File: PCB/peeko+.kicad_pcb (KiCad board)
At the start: 2 copper layers, 52.1 x 43.2 mm, 31 parts, among them J1 Rasberry PI Pico, J2 Conn_02x15_Odd_Even, J3 Conn_01x02_Pin, J4 Conn_01x02_Pin, U1 TXU0104, U2 TXU0104, U3 TXU0104, U4 TXU0104, U5 TXU0104, U6 TXU0104

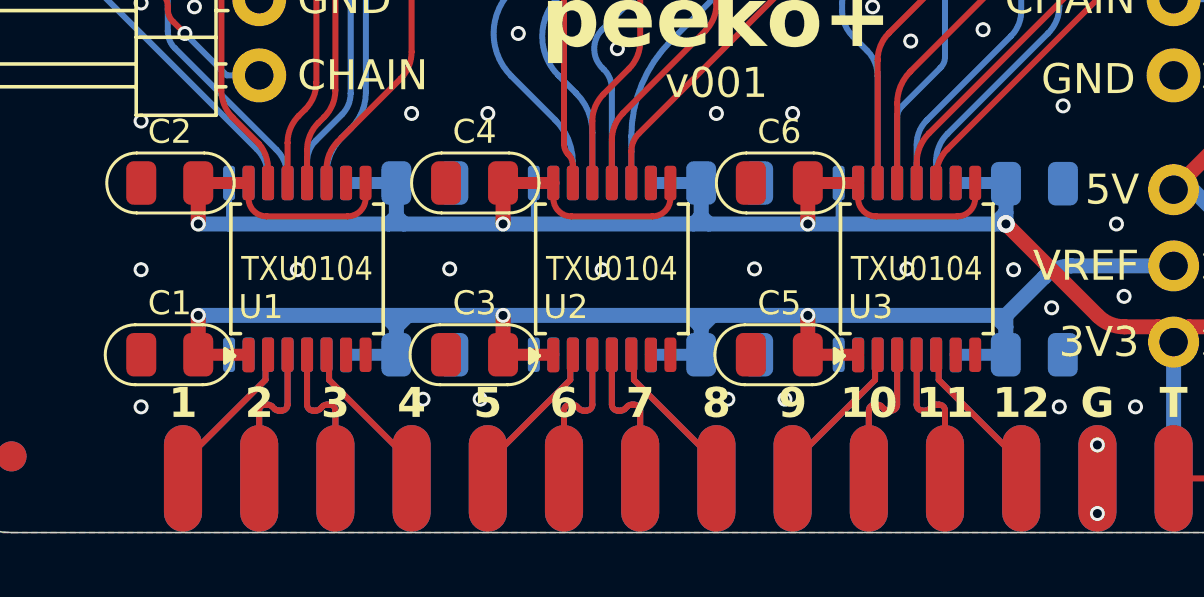
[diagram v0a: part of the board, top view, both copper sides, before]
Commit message: local tssop14 footprint, redo short side traces on peeko+ & level shifter
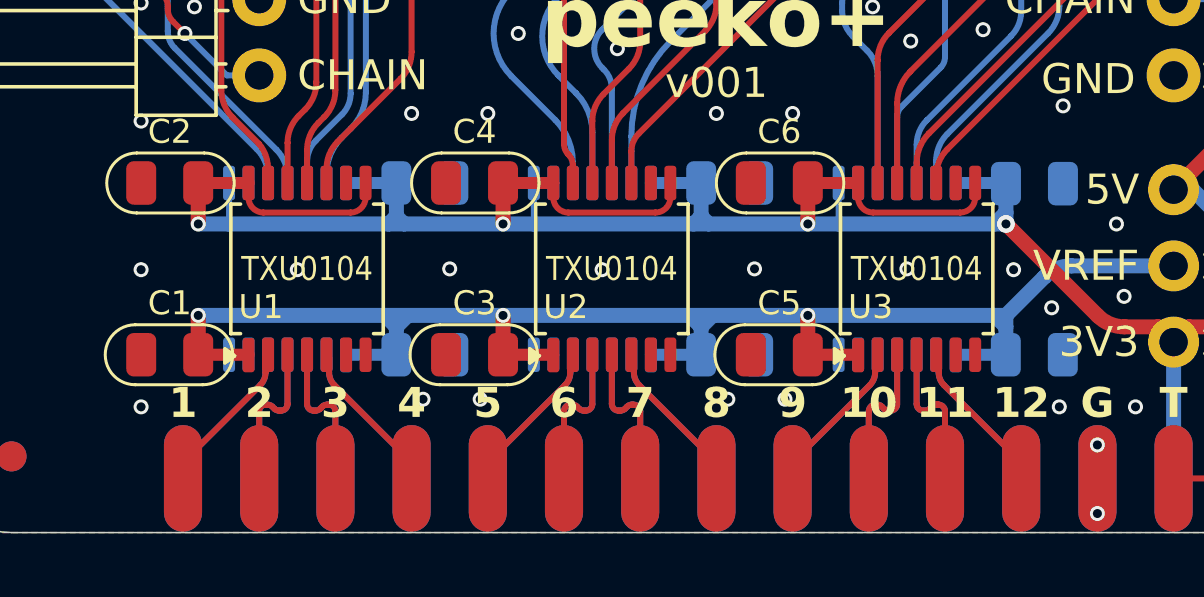
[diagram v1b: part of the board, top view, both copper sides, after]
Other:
- board text added: "5.14"

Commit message: peeko+ housing render
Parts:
- added N1: Housing, 000_LOCAL:peeko+_housing, F.Cu at (146.0, 104.4)
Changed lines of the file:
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@@
 		(pad_to_mask_clearance 0)
 		(allow_soldermask_bridges_in_footprints no)
-		(grid_origin 146.0145 95.4995)
+		(grid_origin 146.0145 104.3895)
 		(pcbplotparams
 			(layerselection 0x00010fc_ffffffff)
@@
 			)
 			(scale
+				(xyz 1 1 1)
+			)
+			(rotate
+				(xyz 0 0 0)
+			)
+		)
+	)
+	(footprint "000_LOCAL:peeko+_housing"
+		(layer "F.Cu")
+		(at 146.0145 104.3895)
+		(property "Reference" "N1"
+			(at 0 1.016 0)
+			(unlocked yes)
+			(layer "Dwgs.User")
+			(effects
+				(font
+					(size 1 1)
+					(thickness 0.15)
+				)
+			)
+		)
+		(property "Value" "Housing"
+			(at 0 2.413 0)
+			(unlocked yes)
+			(layer "F.Fab")
+			(effects
+				(font
+					(size 1 1)
+					(thickness 0.15)
+				)
+			)
+		)
+		(property "Footprint" "000_LOCAL:peeko+_housing"
+			(at 0 0 0)
+			(unlocked yes)
+			(layer "F.Fab")
+			(hide yes)
+			(effects
+				(font
+					(size 1 1)
+					(thickness 0.15)
+				)
+			)
+		)
+		(property "Datasheet" ""
+			(at 0 0 0)
+			(unlocked yes)
+			(layer "F.Fab")
+			(hide yes)
+			(effects
+				(font
+					(size 1 1)
+					(thickness 0.15)
+				)
+			)
+		)
+		(property "Description" "Housing"
+			(at 0 0 0)
+			(unlocked yes)
+			(layer "F.Fab")
+			(hide yes)
+			(effects
+				(font
+					(size 1 1)
+					(thickness 0.15)
+				)
+			)
+		)
+		(property ki_fp_filters "Enclosure* Housing*")
+		(sheetname "Root")
+		(sheetfile "peeko+.kicad_sch")
+		(attr exclude_from_pos_files allow_missing_courtyard)
+		(model "${KIPRJMOD}/000_LOCAL.pretty/3d/peeko+_housing.step"
+			(offset
+				(xyz 0 0 -1.6)
+			)
+			(scale
